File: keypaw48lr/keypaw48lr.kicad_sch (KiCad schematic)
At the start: 0 parts

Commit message: feat: add leds and paw3395 to schema
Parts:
- added C10, C12, C6, C8: 100nF, Capacitor_SMD:C_0805_2012Metric, symbol Device:C
- added C11, C5, C9: 10uF, Capacitor_SMD:C_0805_2012Metric, symbol Device:C
- added C13, C3, C4: 1uF, Capacitor_SMD:C_0805_2012Metric, symbol Device:C
- added C7: 4.7uF, Capacitor_SMD:C_0805_2012Metric, symbol Device:C
- added D1, D10, D11, D12, D13, D14, D15, D16, D17, D18, D19, D2, D20, D21, D22, D23, D24, D3, D4, D5, D6, D7, D8, D9: WS2812B, WS2812B_2020_V6:LED_WS2812B-2020_backmount_rev, symbol WS2812B_2020_V6:WS2812B-2020-V6
- added R1: 10k, Resistor_SMD:R_0805_2012Metric, symbol Device:R
- added R2: 2M, Resistor_SMD:R_0805_2012Metric, symbol Device:R
- added R3: 5.6R, Resistor_SMD:R_0805_2012Metric, symbol Device:R
- added U1: nice_nano, PCM_marbastlib-xp-promicroish:nice_nano_AH_USBup, symbol marbastlib-promicroish:nice_nano
- added U2: TLV70019_SOT23-5, Package_TO_SOT_SMD:SOT-23-5, symbol Regulator_Linear:TLV70019_SOT23-5
- added U3: TPS22917DBV, Package_TO_SOT_SMD:SOT-23-6, symbol Power_Management:TPS22917DBV
- added U4: PAW3395, paw3395_pcb:PAW3395, symbol Motion_sensor:paw3395
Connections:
- new net: D17.1 (DOUT), D18.3 (DIN)
- new net: D16.1 (DOUT), D17.3 (DIN)
- new net: D18.1 (DOUT), D19.3 (DIN)
- new net: D1.1 (DOUT), D2.3 (DIN)
- new net: D21.1 (DOUT), D22.3 (DIN)
- new net: D20.1 (DOUT), D21.3 (DIN)
- new net: R2.2, U4.14 (Nreset)
- new net: D6.1 (DOUT), D7.3 (DIN)
- new net: D5.1 (DOUT), D6.3 (DIN)
- new net: D7.1 (DOUT), D8.3 (DIN)
- new net: D19.1 (DOUT), D20.3 (DIN)
- new net: D2.1 (DOUT), D3.3 (DIN)
- new net: D15.1 (DOUT), D16.3 (DIN)
- new net: D4.1 (DOUT), D5.3 (DIN)
- new net: D3.1 (DOUT), D4.3 (DIN)
- new net: C7.1, C8.1, U4.5 (VDDREG)
- new net: D11.1 (DOUT), D12.3 (DIN)
- new net: D10.1 (DOUT), D11.3 (DIN)
- new net: D22.1 (DOUT), D23.3 (DIN)
- new net: D14.1 (DOUT), D15.3 (DIN)
- new net: D10.3 (DIN), D9.1 (DOUT)
- new net: D8.1 (DOUT), D9.3 (DIN)
- new net: D13.1 (DOUT), D14.3 (DIN)
- new net: D23.1 (DOUT), D24.3 (DIN)
- new net: D12.1 (DOUT), D13.3 (DIN)
- new net: R3.2, U4.15 (LED_P)
- new net +1V9: C11.1, C12.1, C4.1, C5.1, C6.1, R3.1, U2.5 (OUT), U4.4 (VDD)
- new net +3.3V: C10.1, C13.1, C3.1, C9.1, R1.2, R2.1, U1.16 (3V3), U2.1 (IN), U2.3 (EN), U3.1 (VIN), U4.7 (VDDIO)
- new net +BATT: U1.13 (BAT+), U1.29 (BAT+)
- new net COL0: U1.22 (P1.11-LF)
- new net COL1: U1.21 (P1.13-LF)
- new net COL2: U1.20 (P1.15-LF)
- new net COL3: U1.19 (P0.02-LF)
- new net COL4: U1.18 (P0.29-LF)
- new net COL5: U1.17 (P0.31-LF)
- new net CS_OLED: U1.9 (P1.00)
- new net CS_PAW: U1.7 (P0.22), U4.13 (NCS)
- new net DS_OLED: U1.10 (P0.11)
- new net GND: C10.2, C11.2, C12.2, C13.2, C3.2, C4.2, C5.2, C6.2, C7.2, C8.2, C9.2, D1.2 (VSS), D10.2 (VSS), D11.2 (VSS), D12.2 (VSS), D13.2 (VSS), D14.2 (VSS), D15.2 (VSS), D16.2 (VSS), D17.2 (VSS), D18.2 (VSS), D19.2 (VSS), D2.2 (VSS), D20.2 (VSS), D21.2 (VSS), D22.2 (VSS), D23.2 (VSS), D24.2 (VSS), D3.2 (VSS), D4.2 (VSS), D5.2 (VSS), D6.2 (VSS), D7.2 (VSS), D8.2 (VSS), D9.2 (VSS), U1.14 (GND), U1.3 (GND), U1.4 (GND), U2.2 (GND), U3.2 (GND), U4.3 (GND), U4.8 (VDDIO_GND)
- new net LED: D1.3 (DIN), U1.1 (P0.06)
- new net LED+: D1.4 (VDD), D10.4 (VDD), D11.4 (VDD), D12.4 (VDD), D13.4 (VDD), D14.4 (VDD), D15.4 (VDD), D16.4 (VDD), D17.4 (VDD), D18.4 (VDD), D19.4 (VDD), D2.4 (VDD), D20.4 (VDD), D21.4 (VDD), D22.4 (VDD), D23.4 (VDD), D24.4 (VDD), D3.4 (VDD), D4.4 (VDD), D5.4 (VDD), D6.4 (VDD), D7.4 (VDD), D8.4 (VDD), D9.4 (VDD), U3.5 (QOD), U3.6 (VOUT)
- new net LED_EN: U1.25 (P1.01-LF), U3.3 (ON)
- new net MOTION: U1.8 (P0.24), U4.9 (Motion)
- new net ROW0: U1.23 (P0.10-LF)
- new net ROW1: U1.24 (P0.09-LF)
- new net ROW2: U1.12 (P1.06-LF)
- new net ROW3: U1.11 (P1.04-LF)
- new net SCK: U1.2 (P0.08), U4.10 (SCLK)
- new net SDI: R1.1, U1.6 (P0.20), U4.12 (MISO)
- new net SDO: U1.5 (P0.17), U4.11 (MOSI)
- no-connect marks 0 -> 6
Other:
- note added: "RGB LEDs (WS2812B-V6 can be powered with 3.3V) With load switch to save power"
- note added: "Trackball sensor Using a tricky 1.9V VDD for PAW3395."

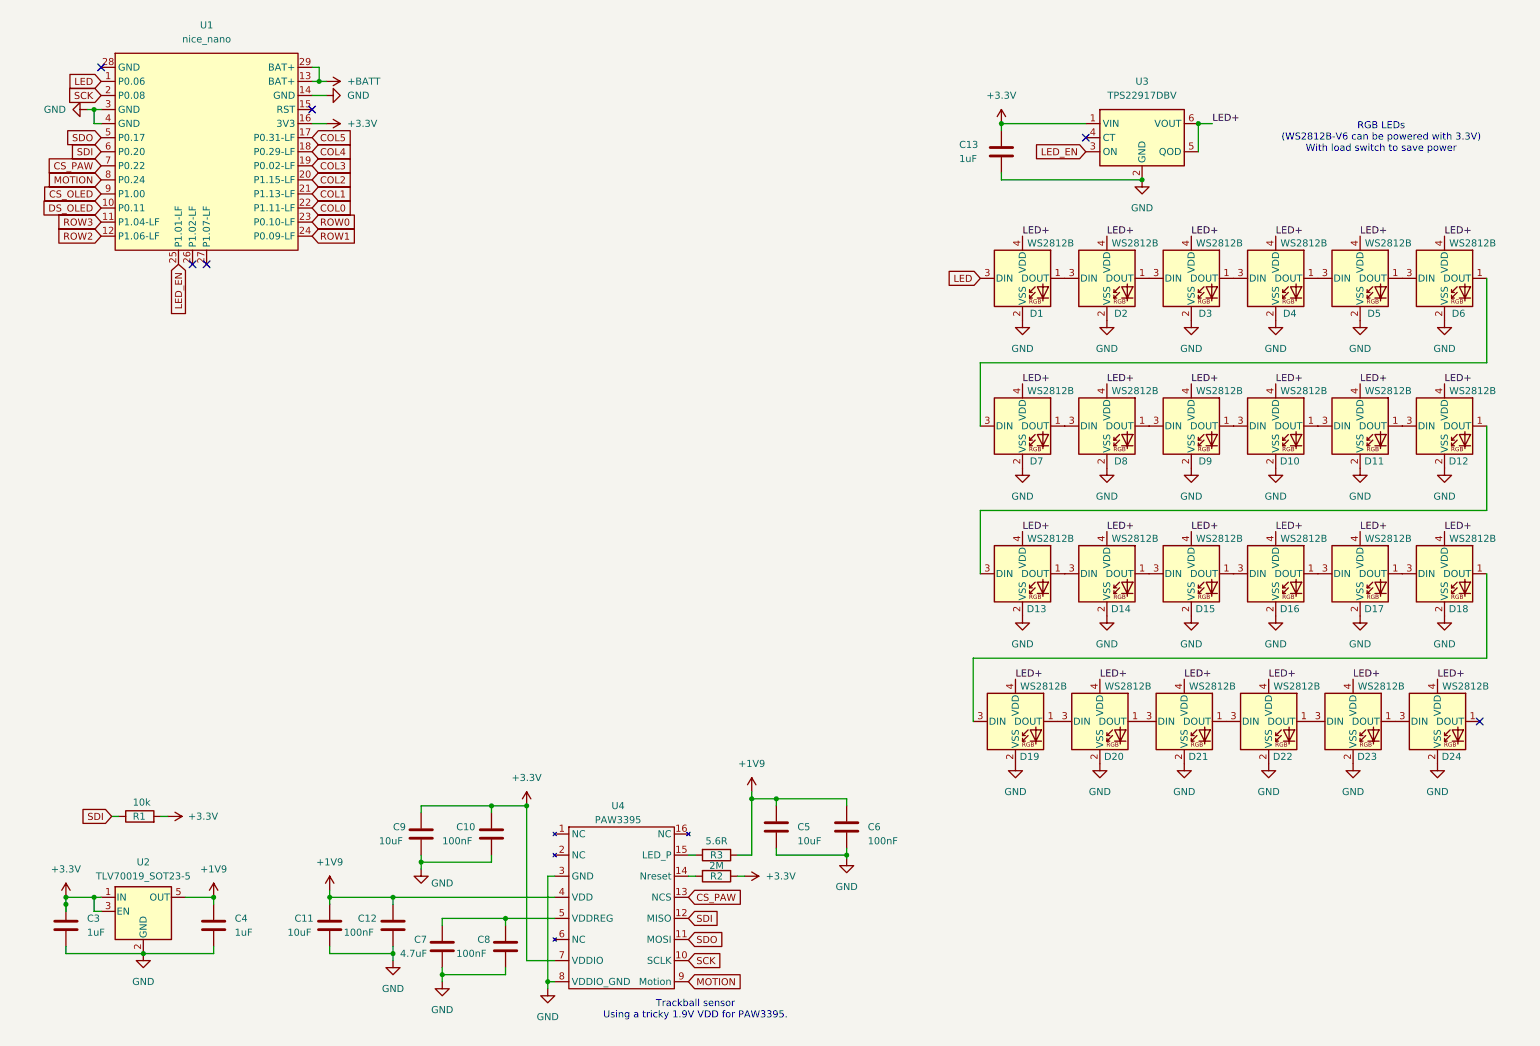
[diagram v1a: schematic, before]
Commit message: feat: complete basic schematic design
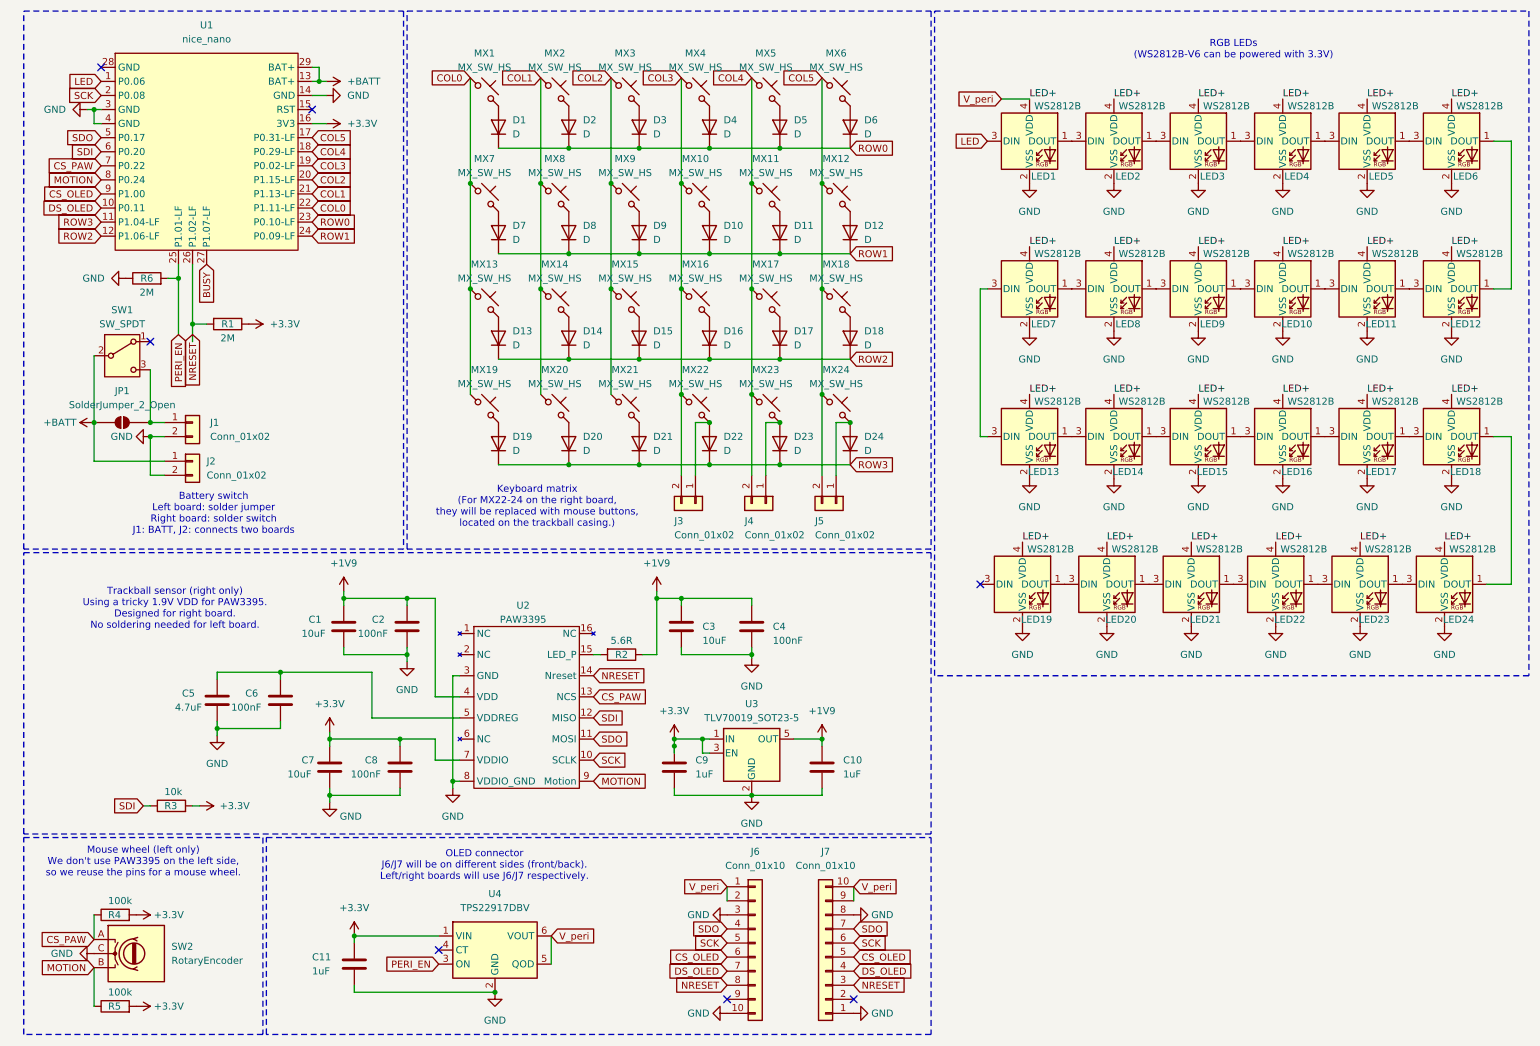
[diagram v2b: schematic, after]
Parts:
- removed R2: 2M, Resistor_SMD:R_0805_2012Metric, symbol Device:R
- added D1, D10, D11, D12, D13, D14, D15, D16, D17, D18, D19, D2, D20, D21, D22, D23, D24, D3, D4, D5, D6, D7, D8, D9: D, MX_SW_HS_REV:D_SOD-323_HandSoldering_REV, symbol Device:D
- added J1, J2, J3, J4, J5: Conn_01x02, Connector_Molex:Molex_PicoBlade_53048-0210_1x02_P1.25mm_Horizontal, symbol Connector_Generic:Conn_01x02
- added J6, J7: Conn_01x10, Connector_FFC-FPC:TE_1-1734839-0_1x10-1MP_P0.5mm_Horizontal, symbol Connector_Generic:Conn_01x10
- added JP1: SolderJumper_2_Open, Jumper:SolderJumper-2_P1.3mm_Open_TrianglePad1.0x1.5mm, symbol Jumper:SolderJumper_2_Open
- added MX1, MX10, MX11, MX12, MX13, MX14, MX15, MX16, MX17, MX18, MX19, MX2, MX20, MX21, MX22, MX23, MX24, MX3, MX4, MX5, MX6, MX7, MX8, MX9: MX_SW_HS, MX_SW_HS_REV:SW_MX_HS_REV, symbol MX_SW_HS_REV:MX_SW_HS_REV
- added R1, R6: 2M, Resistor_SMD:R_1206_3216Metric_Pad1.30x1.75mm_HandSolder, symbol Device:R
- added R4, R5: 100k, Resistor_SMD:R_1206_3216Metric_Pad1.30x1.75mm_HandSolder, symbol Device:R
- added SW1: SW_SPDT, Button_Switch_SMD:SW_SPDT_CK_JS102011SAQN, symbol Switch:SW_SPDT
- added SW2: RotaryEncoder, ALPS_EC10E:RotaryEncoder_Alps_EC10E-Switch, symbol Device:RotaryEncoder
- C1: renamed from C11; footprint Capacitor_SMD:C_0805_2012Metric -> Capacitor_SMD:C_1206_3216Metric_Pad1.33x1.80mm_HandSolder
- C10: renamed from C4; footprint Capacitor_SMD:C_0805_2012Metric -> Capacitor_SMD:C_1206_3216Metric_Pad1.33x1.80mm_HandSolder
- C11: renamed from C13; footprint Capacitor_SMD:C_0805_2012Metric -> Capacitor_SMD:C_1206_3216Metric_Pad1.33x1.80mm_HandSolder
- C2: renamed from C12; footprint Capacitor_SMD:C_0805_2012Metric -> Capacitor_SMD:C_0805_2012Metric_Pad1.18x1.45mm_HandSolder
- C3: renamed from C5; footprint Capacitor_SMD:C_0805_2012Metric -> Capacitor_SMD:C_1206_3216Metric_Pad1.33x1.80mm_HandSolder
- C4: renamed from C6; footprint Capacitor_SMD:C_0805_2012Metric -> Capacitor_SMD:C_0805_2012Metric_Pad1.18x1.45mm_HandSolder
- C5: renamed from C7; footprint Capacitor_SMD:C_0805_2012Metric -> Capacitor_SMD:C_1206_3216Metric_Pad1.33x1.80mm_HandSolder
- C6: renamed from C8; footprint Capacitor_SMD:C_0805_2012Metric -> Capacitor_SMD:C_0805_2012Metric_Pad1.18x1.45mm_HandSolder
- C7: renamed from C9; footprint Capacitor_SMD:C_0805_2012Metric -> Capacitor_SMD:C_1206_3216Metric_Pad1.33x1.80mm_HandSolder
- C8: renamed from C10; footprint Capacitor_SMD:C_0805_2012Metric -> Capacitor_SMD:C_0805_2012Metric_Pad1.18x1.45mm_HandSolder
- C9: renamed from C3; footprint Capacitor_SMD:C_0805_2012Metric -> Capacitor_SMD:C_1206_3216Metric_Pad1.33x1.80mm_HandSolder
- R2: renamed from R3; footprint Resistor_SMD:R_0805_2012Metric -> Resistor_SMD:R_1206_3216Metric_Pad1.30x1.75mm_HandSolder
- R3: renamed from R1; footprint Resistor_SMD:R_0805_2012Metric -> Resistor_SMD:R_1206_3216Metric_Pad1.30x1.75mm_HandSolder
- U3: renamed from U2; footprint Package_TO_SOT_SMD:SOT-23-5 -> Package_TO_SOT_SMD:SOT-23-5_HandSoldering
- U4: renamed from U3; footprint Package_TO_SOT_SMD:SOT-23-6 -> Package_TO_SOT_SMD:SOT-23-6_Handsoldering
- renumbered D1 to LED1, D10 to LED10, D11 to LED11, D12 to LED12, D13 to LED13, D14 to LED14, D15 to LED15, D16 to LED16, D17 to LED17, D18 to LED18, D19 to LED19, D2 to LED2, D20 to LED20, D21 to LED21, D22 to LED22, D23 to LED23, D24 to LED24, D3 to LED3, D4 to LED4, D5 to LED5, D6 to LED6, D7 to LED7, D8 to LED8, D9 to LED9, U4 to U2
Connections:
- net +3.3V: now also R1.1, R4.2, R5.2
- net +BATT: now also J2.1 (Pin_1), JP1.1 (A), SW1.2 (B)
- net COL0: now also MX1.1, MX13.1, MX19.1, MX7.1
- net COL1: now also MX14.1, MX2.1, MX20.1, MX8.1
- net COL2: now also MX15.1, MX21.1, MX3.1, MX9.1
- net COL3: now also J3.2 (Pin_2), MX10.1, MX16.1, MX22.1, MX4.1
- net COL4: now also J4.2 (Pin_2), MX11.1, MX17.1, MX23.1, MX5.1
- net COL5: now also J5.2 (Pin_2), MX12.1, MX18.1, MX24.1, MX6.1
- net CS_OLED: now also J6.6 (Pin_6), J7.5 (Pin_5)
- net CS_PAW: now also R4.1, SW2.A
- net DS_OLED: now also J6.7 (Pin_7), J7.4 (Pin_4)
- net GND: now also J1.2 (Pin_2), J2.2 (Pin_2), J6.10 (Pin_10), J6.3 (Pin_3), J7.1 (Pin_1), J7.8 (Pin_8), R6.1, SW2.C
- net MOTION: now also R5.1, SW2.B
- net ROW0: now also D1.1 (K), D2.1 (K), D3.1 (K), D4.1 (K), D5.1 (K), D6.1 (K)
- net ROW1: now also D10.1 (K), D11.1 (K), D12.1 (K), D7.1 (K), D8.1 (K), D9.1 (K)
- net ROW2: now also D13.1 (K), D14.1 (K), D15.1 (K), D16.1 (K), D17.1 (K), D18.1 (K)
- net ROW3: now also D19.1 (K), D20.1 (K), D21.1 (K), D22.1 (K), D23.1 (K), D24.1 (K)
- net SCK: now also J6.5 (Pin_5), J7.6 (Pin_6)
- net SDO: now also J6.4 (Pin_4), J7.7 (Pin_7)
- net at LED18.1 (DOUT): now also LED24.1 (DOUT); no longer LED19.3 (DIN)
- net NRESET: now reaches U2.14 (Nreset)
- net NRESET: now also U1.26 (P1.02-LF), J6.8 (Pin_8), J7.3 (Pin_3), R1.2
- net at LED6.1 (DOUT): now also LED12.1 (DOUT); no longer LED7.3 (DIN)
- net BUSY: now reaches U1.27 (P1.07-LF)
- net at LED13.3 (DIN): now also LED7.3 (DIN); no longer LED12.1 (DOUT)
- net LED+ renamed V_peri
- net V_peri: now also J6.1 (Pin_1), J6.2 (Pin_2), J7.10 (Pin_10), J7.9 (Pin_9)
- net LED_EN renamed PERI_EN
- net PERI_EN: now also R6.2
- new net: D24.2 (A), J5.1 (Pin_1), MX24.2
- new net: D3.2 (A), MX3.2
- new net: D7.2 (A), MX7.2
- new net: D10.2 (A), MX10.2
- new net: D2.2 (A), MX2.2
- new net: D4.2 (A), MX4.2
- new net: D22.2 (A), J3.1 (Pin_1), MX22.2
- new net: D16.2 (A), MX16.2
- new net: D20.2 (A), MX20.2
- new net: D17.2 (A), MX17.2
- new net: D5.2 (A), MX5.2
- new net: D14.2 (A), MX14.2
- new net: D23.2 (A), J4.1 (Pin_1), MX23.2
- new net: D6.2 (A), MX6.2
- new net: D18.2 (A), MX18.2
- new net: D21.2 (A), MX21.2
- new net: D15.2 (A), MX15.2
- new net: D12.2 (A), MX12.2
- new net: D9.2 (A), MX9.2
- new net: D11.2 (A), MX11.2
- new net: D19.2 (A), MX19.2
- new net: D1.2 (A), MX1.2
- new net: D13.2 (A), MX13.2
- new net: D8.2 (A), MX8.2
- new net: J1.1 (Pin_1), JP1.2 (B), SW1.3 (C)
- no-connect marks 6 -> 7
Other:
- note added: "Battery switch Left board: solder jumper Right board: solder switch J1: BATT, J2: connects two boards"
- note added: "Keyboard matrix (For MX22-24 on the right board, they will be replaced with mouse buttons, located on the trackball casing.)"
- note added: "Mouse wheel (left only) We don't use PAW3395 on the left side, so we reuse the pins for a mouse wheel."
- note added: "OLED connector J6/J7 will be on different sides (front/back). Left/right boards will use J6/J7 respectively."
- note added: "RGB LEDs (WS2812B-V6 can be powered with 3.3V)"
- note added: "Trackball sensor (right only) Using a tricky 1.9V VDD for PAW3395. Designed for right board. No soldering needed for left board."
- note removed: "RGB LEDs (WS2812B-V6 can be powered with 3.3V) With load switch to save power"
- note removed: "Trackball sensor Using a tricky 1.9V VDD for PAW3395."
- moved on the sheet: C1, C10, C11, C2, C3, C4, C5, C6, C7, C8, C9, LED1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

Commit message: feat: add symbol/footprint for OLED screen
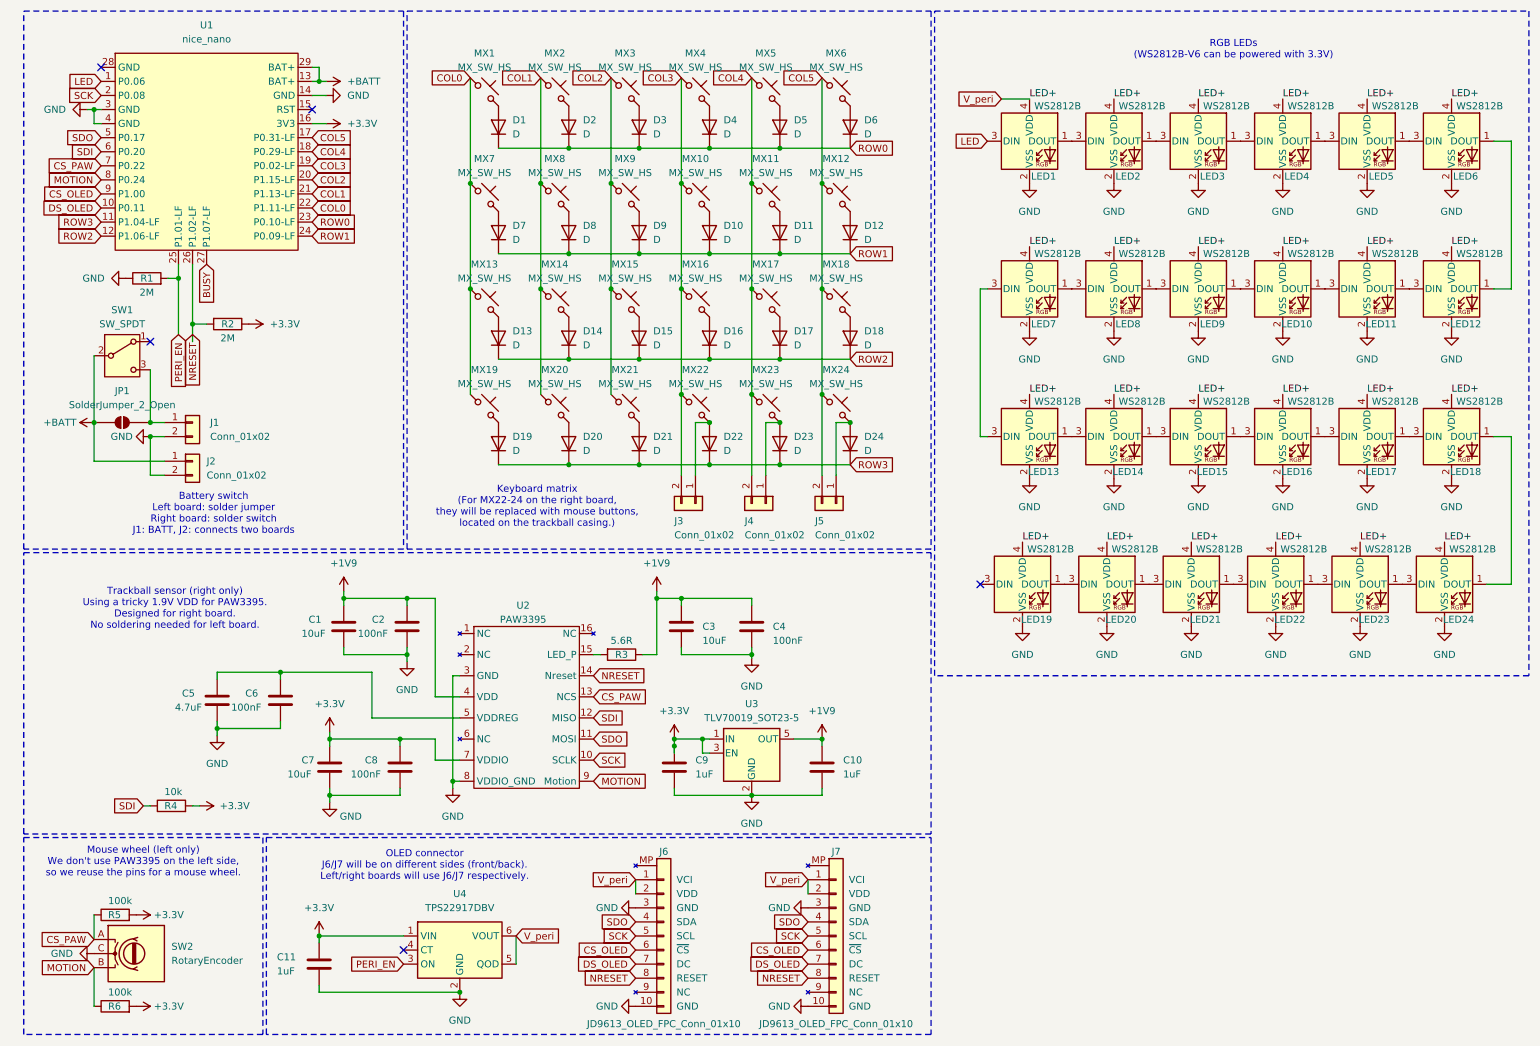
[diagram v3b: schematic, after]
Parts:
- removed J6, J7: Conn_01x10, Connector_FFC-FPC:TE_1-1734839-0_1x10-1MP_P0.5mm_Horizontal, symbol Connector_Generic:Conn_01x10
- added J6, J7: JD9613_OLED_FPC_Conn_01x10, JD9613_OLED_FPC:TE_1-1734839-0_1x10-1MP_P0.5mm_Horizontal, symbol JD9613_OLED_FPC:JD9613_OLED_FPC_Conn_01x10
- renumbered R6 to R1, R1 to R2, R2 to R3, R3 to R4, R4 to R5, R5 to R6
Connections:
- net CS_OLED: now also J6.6 (~{CS}), J7.6 (~{CS})
- net DS_OLED: now also J6.7 (DC), J7.7 (DC)
- net GND: now also J6.10 (GND), J6.3 (GND), J7.10 (GND), J7.3 (GND)
- net NRESET: now also J6.8 (RESET), J7.8 (RESET)
- net SCK: now also J6.5 (SCL), J7.5 (SCL)
- net SDO: now also J6.4 (SDA), J7.4 (SDA)
- net V_peri: now also J6.1 (VCI), J6.2 (VDD), J7.1 (VCI), J7.2 (VDD)
- no-connect marks 7 -> 5
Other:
- moved on the sheet: C11, U4
